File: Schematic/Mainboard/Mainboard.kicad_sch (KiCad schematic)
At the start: 1 part, among them U1 BP

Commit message: updates to CAD and schematic
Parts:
- added J1: Motor_C, symbol Connector_Generic:Conn_01x02
- added J2: Motor_B, symbol Connector_Generic:Conn_01x02
- added J3: Motor_A, symbol Connector_Generic:Conn_01x02
- added J4: Servo, symbol Connector_Generic:Conn_01x03
- added U2, U3: ~, My_Library:HW-627, symbol My_Library:HW-627
- added U4: XL60019_Boost_Module, My_Library:Mini360, symbol My_Library:XL60019_Boost_Module
- added U5: Mini360, My_Library:Mini360, symbol My_Library:Mini360
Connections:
- net +3V3: now reaches U1.3V3 (3.3V)
- net +3V3: now also U5.4 (OUT)
- net GND: now reaches U1.G (GND)
- net GND: now also U4.1 (GND), U4.3 (GND), U5.1 (GND), U5.3 (GND)
- new net +12V: U4.4 (OUT)
- new net +BATT: U4.2 (IN), U5.2 (IN)
- no-connect marks 0 -> 5
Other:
- moved on the sheet: U1

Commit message: more schematic updates
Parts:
- added J5: Servo, Connector_PinHeader_2.54mm:PinHeader_1x03_P2.54mm_Vertical, symbol Connector_Generic:Conn_01x03
- added J6: ESC, Connector_PinHeader_2.54mm:PinHeader_1x03_P2.54mm_Vertical, symbol Connector_Generic:Conn_01x03
- added J7: ESC_PWR, Connector_PinHeader_2.54mm:PinHeader_1x02_P2.54mm_Vertical, symbol Connector_Generic:Conn_01x02
- added SW1: SW_DIP_x01, Connector_PinHeader_2.54mm:PinHeader_1x02_P2.54mm_Vertical, symbol Switch:SW_DIP_x01
- added U6: RFM69HW, RF_Module:HOPERF_RFM69HW, symbol RF_Module:RFM69HW
- J1, J2, J3: footprint (none) -> Connector_PinHeader_2.54mm:PinHeader_1x02_P2.54mm_Vertical
- J4: footprint (none) -> Connector_PinHeader_2.54mm:PinHeader_1x03_P2.54mm_Vertical
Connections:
- net +12V: now also U2.9 (VMOT), U3.9 (VMOT)
- net +3V3: now also U2.1 (SLEEP), U3.1 (SLEEP), U6.8 (3.3V)
- net +BATT: now also SW1.1; no longer U4.2 (IN), U5.2 (IN)
- net GND: now also J4.3 (Pin_3), U2.10 (GND), U3.10 (GND), J5.3 (Pin_3), J6.3 (Pin_3), J7.2 (Pin_2), U6.11 (GND), U6.9 (GND)
- net at J1.1 (Pin_1): now also U3.3 (OUT2)
- net at J1.2 (Pin_2): now also U3.2 (OUT1)
- net SERVO 1: now reaches J4.1 (Pin_1)
- net SERVO 1: now also U1.PB9
- net +BATT SW: now reaches J4.2 (Pin_2)
- net +BATT SW: now also U4.2 (IN), U5.2 (IN), J5.2 (Pin_2), J7.1 (Pin_1), SW1.2
- net at J2.1 (Pin_1): now also U2.5 (OUT4)
- net at J2.2 (Pin_2): now also U2.4 (OUT3)
- net M B1: now reaches U2.11 (IN3)
- net M B1: now also U1.PA0
- net M B2: now reaches U2.12 (IN4)
- net M B2: now also U1.PA1
- net at U2.2 (OUT1): now also J3.2 (Pin_2)
- net at U2.3 (OUT2): now also J3.1 (Pin_1)
- net M A1: now reaches U2.7 (IN1)
- net M A1: now also U1.PC14
- net M A2: now reaches U2.8 (IN2)
- net M A2: now also U1.PC15
- net M C1: now reaches U1.PA2
- net M C1: now also U3.7 (IN1)
- net M C2: now reaches U1.PA3
- net M C2: now also U3.8 (IN2)
- net NSS: now reaches U1.PA4
- net NSS: now also U6.15 (NSS)
- net SCK: now reaches U1.PA5
- net SCK: now also U6.12 (SCK)
- net MISO: now reaches U1.PA6
- net MISO: now also U6.13 (MISO)
- net MOSI: now reaches U1.PA7
- net MOSI: now also U6.14 (MOSI)
- net AUX: now reaches U1.PB3
- net AUX: now also U6.6 (DIO4)
- net INTER: now reaches U1.PB4
- net INTER: now also U6.2 (DIO0)
- net RESET: now reaches U1.PB5
- net RESET: now also U6.1 (RESET)
- net ESC: now reaches U1.PB7
- net ESC: now also J6.1 (Pin_1)
- net SERVO 2: now reaches U1.PB8
- net SERVO 2: now also J5.1 (Pin_1)
- net SLEEP: now reaches U1.PC13
- no-connect marks 5 -> 32
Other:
- note added: "ESCS"
- note added: "LOGIC SUPPLY"
- note added: "MAIN SWITCH"
- note added: "MOTOR DRIVER"
- note added: "MOTOR SUPPLY"
- note added: "RADIO"
- title: (none) -> Omnidroid Controller
- moved on the sheet: J1, J2, J3, J4, U1, U2, U3

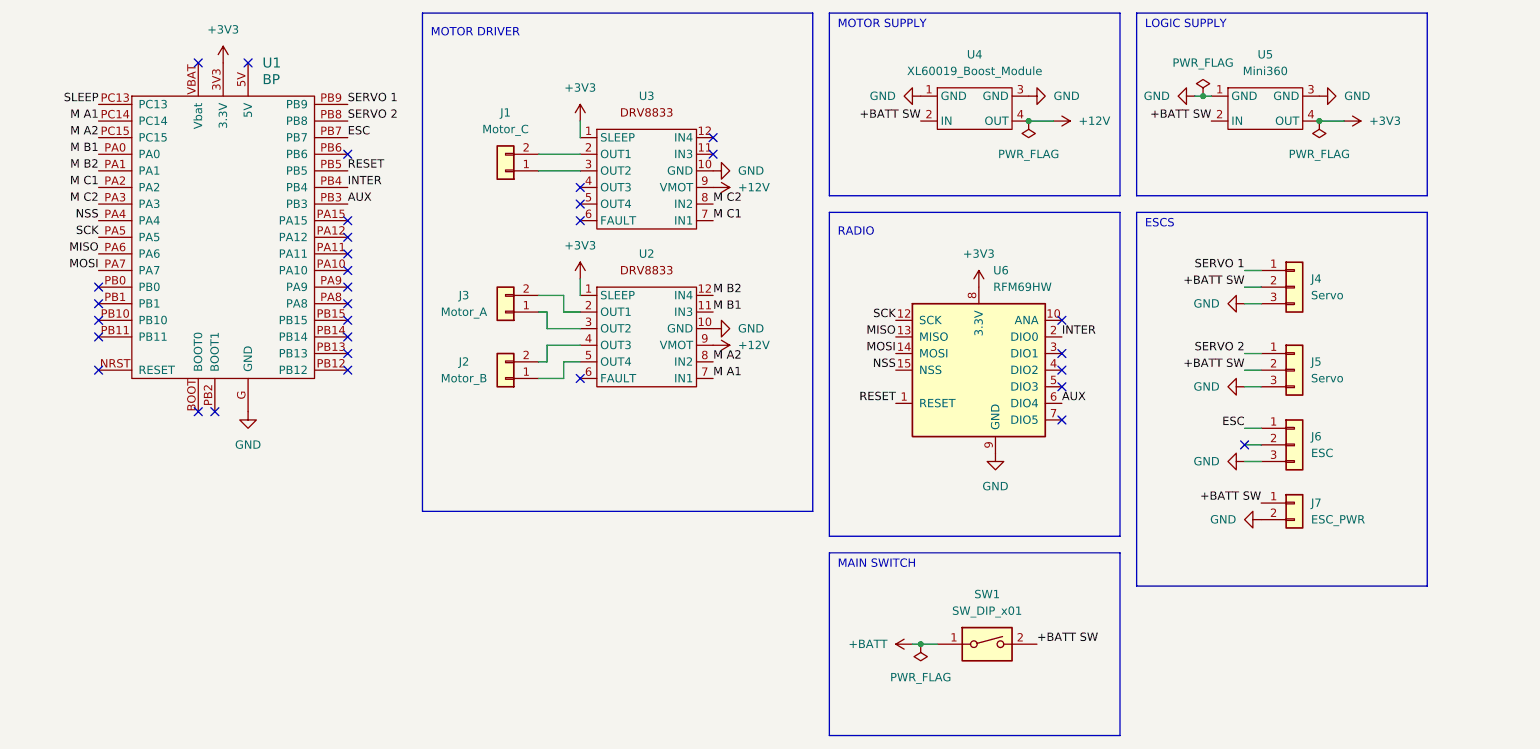
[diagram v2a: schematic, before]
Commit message: PCB work
trying to cram everything on there
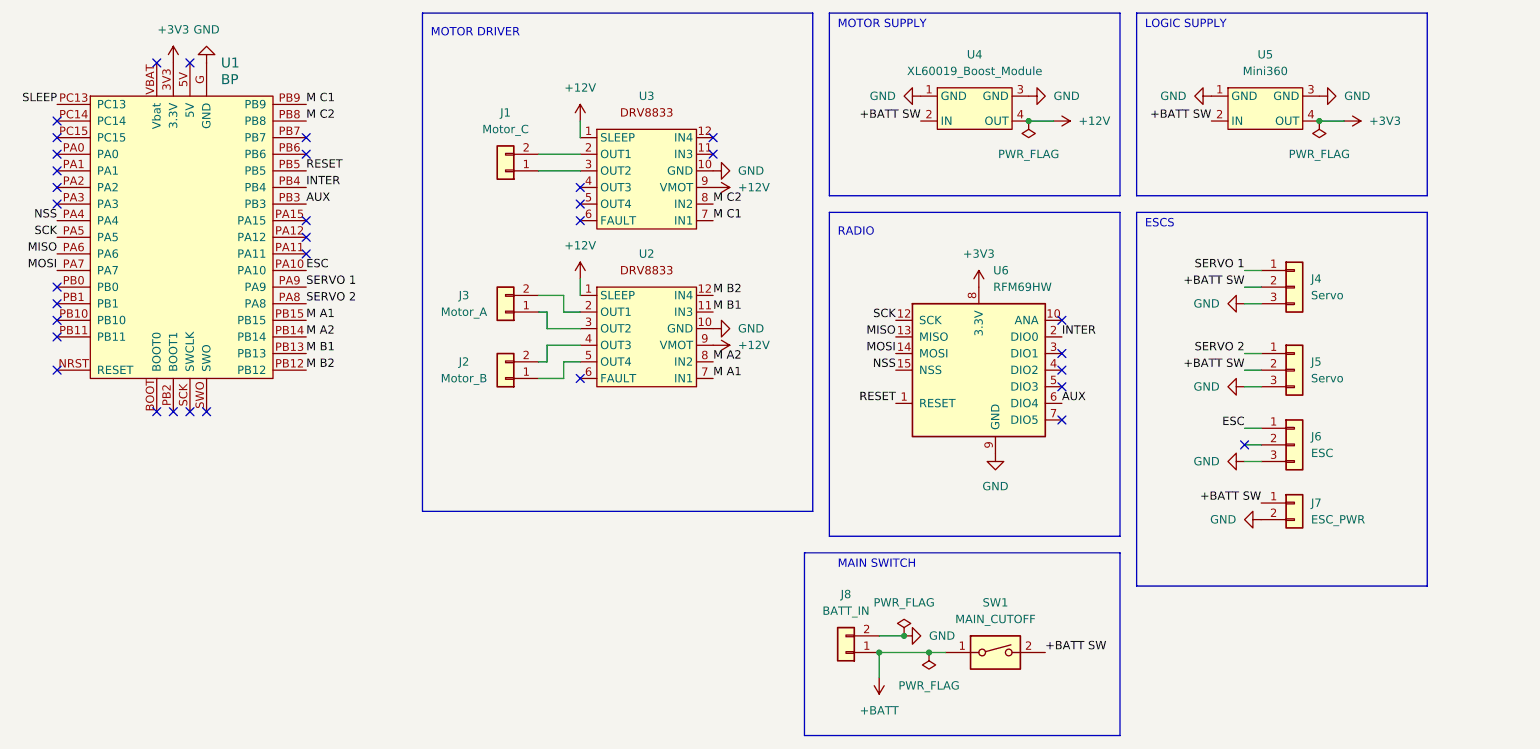
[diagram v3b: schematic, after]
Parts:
- added J8: BATT_IN, Connector_PinHeader_2.54mm:PinHeader_1x02_P2.54mm_Vertical, symbol Connector_Generic:Conn_01x02
- SW1: value SW_DIP_x01 -> MAIN_CUTOFF
- U4: footprint My_Library:Mini360 -> My_Library:XL60019 Boost Module
- U6: footprint RF_Module:HOPERF_RFM69HW -> My_Library:HOPERF_RFM69HW
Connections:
- net +12V: now also U2.1 (SLEEP), U3.1 (SLEEP)
- net +3V3: no longer U2.1 (SLEEP), U3.1 (SLEEP)
- net +BATT: now also J8.1 (Pin_1)
- net ESC: now also U1.PA10; no longer U1.PB7
- net GND: now also J8.2 (Pin_2)
- net M A1: now also U1.PB15; no longer U1.PC14
- net M A2: now also U1.PB14; no longer U1.PC15
- net M B1: now also U1.PB13; no longer U1.PA0
- net M B2: now also U1.PB12; no longer U1.PA1
- net M C1: now also U1.PB9; no longer U1.PA2
- net M C2: now also U1.PB8; no longer U1.PA3
- net SERVO 1: now also U1.PA9; no longer U1.PB9
- net SERVO 2: now also U1.PA8; no longer U1.PB8
- no-connect marks 32 -> 34
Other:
- moved on the sheet: SW1

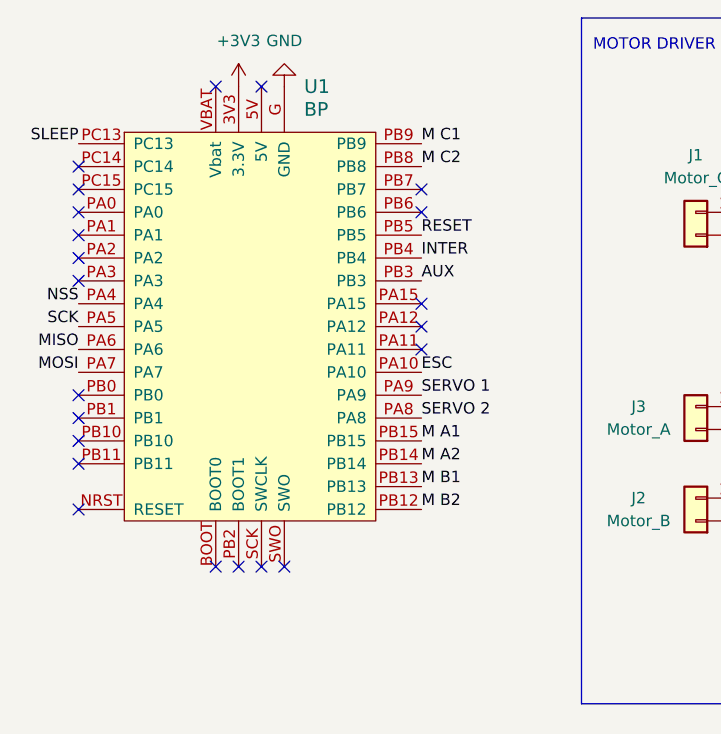
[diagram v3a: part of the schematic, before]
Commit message: shift from STM32 to ESP32
on the robot control surface
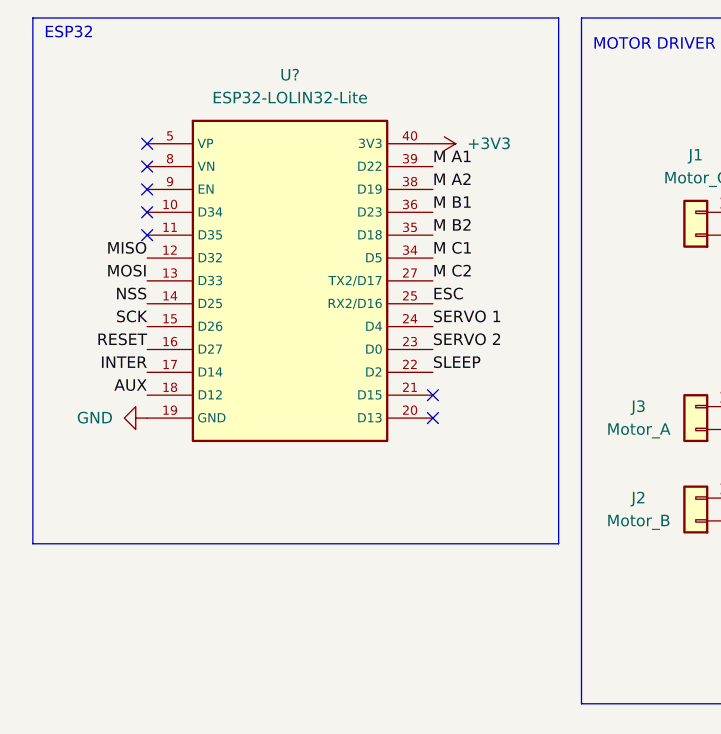
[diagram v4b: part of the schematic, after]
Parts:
- removed U1: BP, My_Library:blue_pill, symbol My_Library:STM32 Bluepill
- added U?: ESP32-LOLIN32-Lite, Espressif:ESP32-LOLIN32-Lite, symbol Espressif:ESP32-LOLIN32-Lite
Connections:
- net +3V3: now also U?.40 (3V3)
- net AUX: now also U?.18 (D12)
- net ESC: now also U?.25 (RX2/D16)
- net GND: now also U?.19 (GND)
- net INTER: now also U?.17 (D14)
- net M A1: now also U?.39 (D22)
- net M A2: now also U?.38 (D19)
- net M B1: now also U?.36 (D23)
- net M B2: now also U?.35 (D18)
- net M C1: now also U?.34 (D5)
- net M C2: now also U?.27 (TX2/D17)
- net MISO: now also U?.12 (D32)
- net MOSI: now also U?.13 (D33)
- net NSS: now also U?.14 (D25)
- net RESET: now also U?.16 (D27)
- net SCK: now also U?.15 (D26)
- net SERVO 1: now also U?.24 (D4)
- net SERVO 2: now also U?.23 (D0)
- net SLEEP: now also U?.22 (D2)
- no-connect marks 34 -> 19
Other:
- note added: "ESP32"

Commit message: finish first revision PCB
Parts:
- added D1: 1N4007, Diode_THT:D_DO-41_SOD81_P7.62mm_Horizontal, symbol Diode:1N4007
- added F1, F2: Fuse 15A, Connector_PinHeader_2.54mm:PinHeader_1x02_P2.54mm_Vertical, symbol Device:Fuse
- renumbered J3 to J1, J1 to J3, J8 to J4, J4 to J5, J5 to J6, J6 to J7, J7 to J8, U3 to U2, U2 to U3, U6 to U4, U4 to U5, U5 to U6
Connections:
- net +12V: now also F2.2; no longer U5.4 (OUT)
- net +BATT SW: now also D1.2 (A), F1.2; no longer SW1.2, U5.2 (IN)
- net M A1: now also U?.27 (TX2/D17); no longer U?.39 (D22)
- net M A2: now also U?.34 (D5); no longer U?.38 (D19)
- net M C1: now also U2.11 (IN3), U?.39 (D22); no longer U2.7 (IN1), U?.34 (D5)
- net M C2: now also U2.12 (IN4), U?.38 (D19); no longer U2.8 (IN2), U?.27 (TX2/D17)
- net MISO: now also U?.14 (D25); no longer U?.12 (D32)
- net NSS: now also U?.12 (D32); no longer U?.14 (D25)
- net SERVO 1: now also U?.23 (D0); no longer U?.24 (D4)
- net SERVO 2: now also U?.24 (D4); no longer U?.23 (D0)
- net at J3.1 (Pin_1): now also U2.5 (OUT4); no longer U2.3 (OUT2)
- net at J3.2 (Pin_2): now also U2.4 (OUT3); no longer U2.2 (OUT1)
- net SLEEP: no longer names the net of U?.22 (D2)
- new net: D1.1 (K), U5.2 (IN)
- new net: F2.1, U5.4 (OUT)
- new net: F1.1, SW1.2
- no-connect marks 19 -> 20
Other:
- moved on the sheet: J3, J4, SW1, U5, U6
